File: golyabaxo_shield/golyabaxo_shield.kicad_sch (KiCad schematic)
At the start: 18 parts, among them J2 Conn_01x09, Q2 Q_NPN_BEC

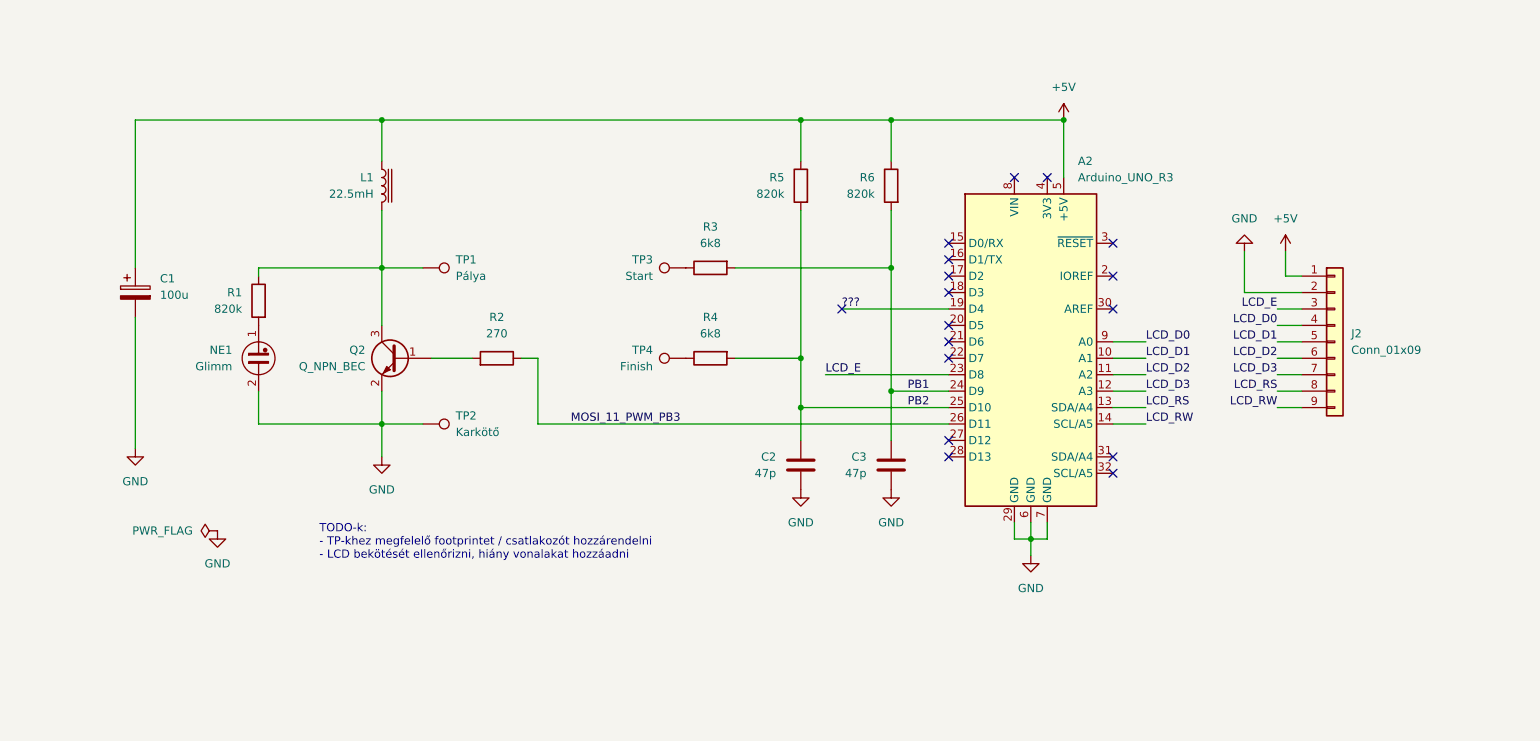
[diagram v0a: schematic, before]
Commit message: Add refurbished firmware for SEMduino-V2 - testing needed
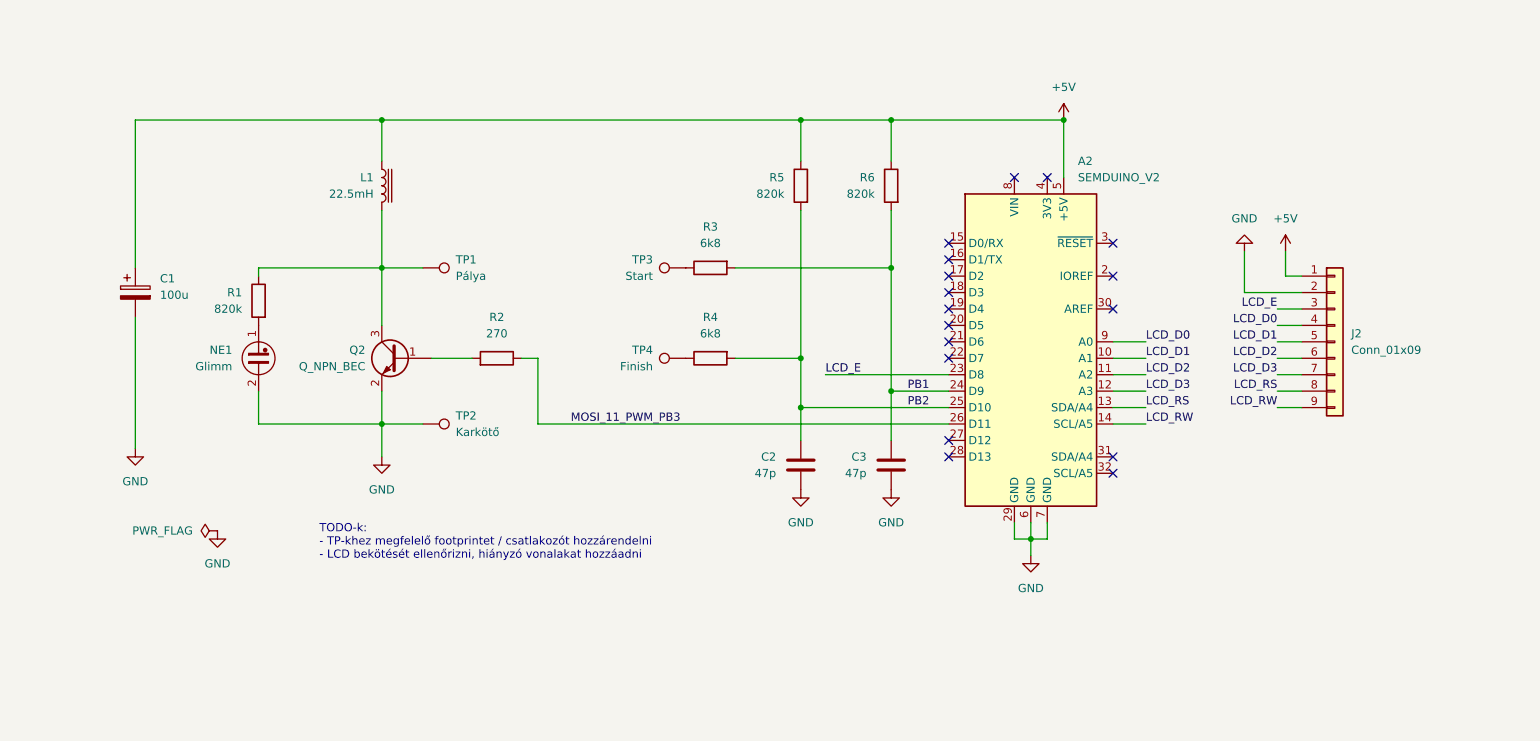
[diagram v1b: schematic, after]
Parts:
- A2: value Arduino_UNO_R3 -> SEMDUINO_V2
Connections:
- net ???: no longer names the net of A2.19 (D4)
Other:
- note added: "TODO-k: - TP-khez megfelelő footprintet / csatlakozót hozzárendelni - LCD bekötését ellenőrizni, hiányzó vonalakat hozzáadni"
- note removed: "TODO-k: - TP-khez megfelelő footprintet / csatlakozót hozzárendelni - LCD bekötését ellenőrizni, hiány vonalakat hozzáadni"
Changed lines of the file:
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@@
-	)
-	(no_connect
-		(at 163.83 92.71)
 	)
 	(no_connect
@@
 	)
 	(no_connect
+		(at 180.34 92.71)
+	)
+	(no_connect
 		(at 190.5 72.39)
 	)
@@
 	(wire
 		(pts
-			(xy 163.83 92.71) (xy 180.34 92.71)
-		)
-		(stroke
-			(width 0)
-			(type default)
-		)
-	)
-	(wire
-		(pts
 			(xy 231.14 92.71) (xy 234.95 92.71)
 		)
@@
 		)
 	)
-	(text "TODO-k:\n- TP-khez megfelelő footprintet / csatlakozót hozzárendelni\n- LCD bekötését ellenőrizni, hiány vonalakat hozzáadni"
+	(text "TODO-k:\n- TP-khez megfelelő footprintet / csatlakozót hozzárendelni\n- LCD bekötését ellenőrizni, hiányzó vonalakat hozzáadni"
 		(exclude_from_sim no)
 		(at 83.058 128.778 0)
@@
 	(label "PB2"
 		(at 173.99 107.95 0)
-		(fields_autoplaced yes)
-		(effects
-			(font
-				(size 1.27 1.27)
-			)
-			(justify left bottom)
-		)
-	)
-	(label "???"
-		(at 163.83 92.71 0)
 		(fields_autoplaced yes)
 		(effects
@@
 			)
 		)
-		(property "Value" "Arduino_UNO_R3"
+		(property "Value" "SEMDUINO_V2"
 			(at 200.3141 72.39 0)
 			(effects

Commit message: Build SEMduino shield
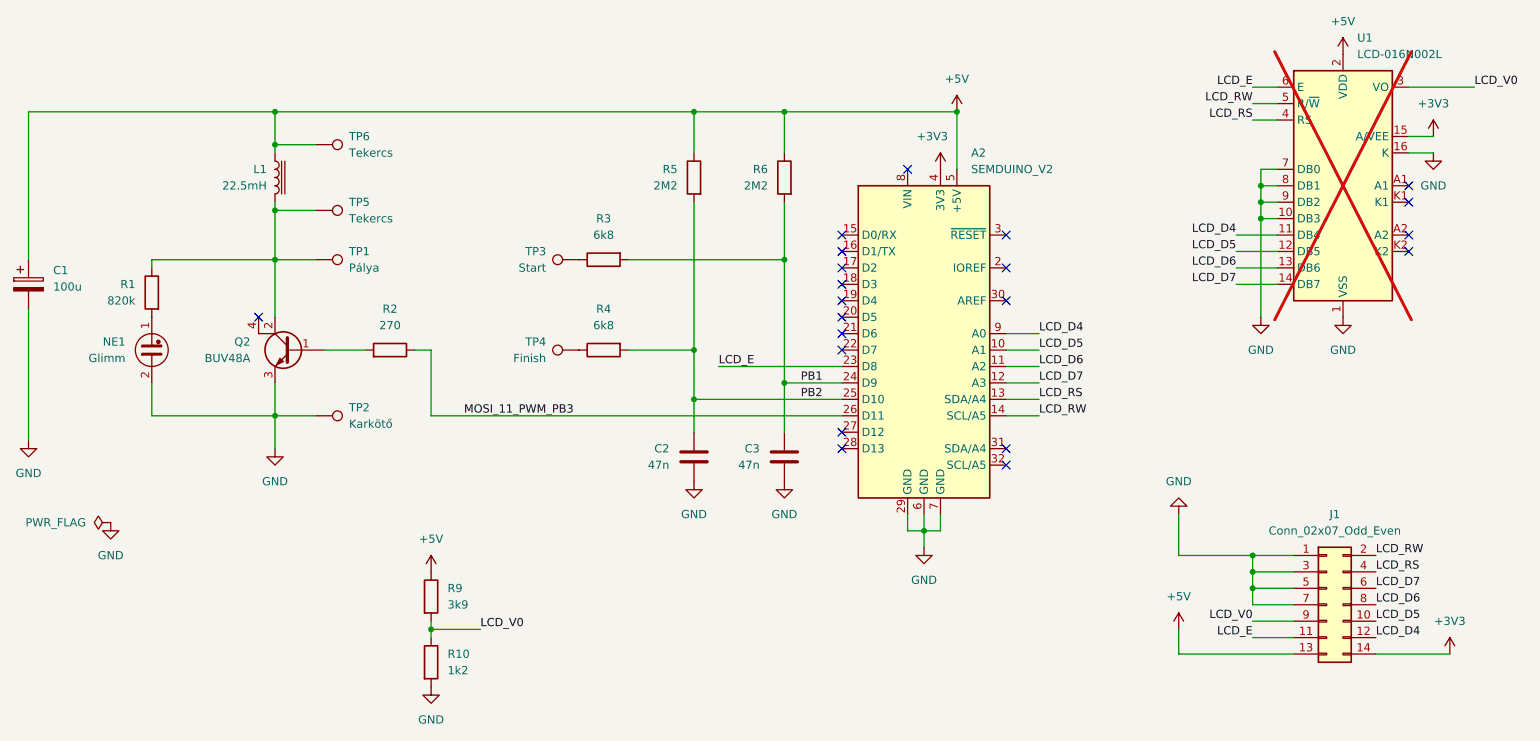
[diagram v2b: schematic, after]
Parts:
- removed J2: Conn_01x09, Connector_PinHeader_2.54mm:PinHeader_1x09_P2.54mm_Horizontal, symbol Connector_Generic:Conn_01x09
- removed Q2: Q_NPN_BEC, Package_TO_SOT_THT:TO-218-3_Horizontal_TabDown, symbol Device:Q_NPN_BEC
- added J1: Conn_02x07_Odd_Even, Connector_PinHeader_2.54mm:PinHeader_2x07_P2.54mm_Vertical_SMD, symbol Connector_Generic:Conn_02x07_Odd_Even
- added Q2: BUV48A, Package_TO_SOT_THT:TO-218-3_Horizontal_TabDown, symbol Device:Q_NPN_BCEC
- added R10: 1k2, Resistor_THT:R_Axial_DIN0207_L6.3mm_D2.5mm_P10.16mm_Horizontal, symbol Device:R
- added R9: 3k9, Resistor_THT:R_Axial_DIN0207_L6.3mm_D2.5mm_P10.16mm_Horizontal, symbol Device:R
- added TP5, TP6: Tekercs, TestPoint:TestPoint_Pad_D2.5mm, symbol Connector:TestPoint
- added U1: LCD-016N002L, Display:LCD-016N002L, symbol Display_Character:LCD-016N002L
- C2, C3: value 47p -> 47n; footprint Capacitor_THT:C_Disc_D4.3mm_W1.9mm_P5.00mm -> Capacitor_THT:C_Disc_D3.8mm_W2.6mm_P2.50mm
- L1: footprint Connector_PinHeader_2.54mm:PinHeader_1x02_P2.54mm_Horizontal -> (none)
- NE1: footprint LED_THT:LED_D5.0mm_Clear -> LED_THT:LED_D5.0mm_IRGrey
- R5, R6: value 820k -> 2M2
- TP1, TP2, TP3, TP4: footprint TestPoint:TestPoint_Loop_D2.50mm_Drill1.0mm -> TestPoint:TestPoint_Pad_D2.5mm
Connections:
- net +5V: now also J1.13 (Pin_13), R9.1, TP6.1, U1.2 (VDD)
- net GND: now also J1.1 (Pin_1), J1.3 (Pin_3), J1.5 (Pin_5), J1.7 (Pin_7), Q2.3 (E), R10.2, U1.1 (VSS), U1.10 (DB3), U1.16 (K), U1.7 (DB0), U1.8 (DB1), U1.9 (DB2)
- net LCD_E: now also J1.11 (Pin_11), U1.6 (E)
- net LCD_RS: now also J1.4 (Pin_4), U1.4 (RS)
- net LCD_RW: now also J1.2 (Pin_2), U1.5 (R/~{W})
- net at L1.1, R1.1, TP1.1: now also Q2.2 (C), TP5.1
- net at R2.2: now also Q2.1 (B)
- net +3V3: now reaches A2.4 (3V3)
- net +3V3: now also J1.14 (Pin_14), U1.15 (A/VEE)
- net LCD_D0 renamed LCD_D4
- net LCD_D4: now also J1.12 (Pin_12), U1.11 (DB4)
- net LCD_D1 renamed LCD_D5
- net LCD_D5: now also J1.10 (Pin_10), U1.12 (DB5)
- net LCD_D2 renamed LCD_D6
- net LCD_D6: now also J1.8 (Pin_8), U1.13 (DB6)
- net LCD_D3 renamed LCD_D7
- net LCD_D7: now also J1.6 (Pin_6), U1.14 (DB7)
- new net LCD_V0: J1.9 (Pin_9), R10.1, R9.2, U1.3 (VO)
- no-connect marks 17 -> 21
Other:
- note removed: "TODO-k: - TP-khez megfelelő footprintet / csatlakozót hozzárendelni - LCD bekötését ellenőrizni, hiányzó vonalakat hozzáadni"
- moved on the sheet: A2, C1, C2, C3, L1, NE1, R1, R2, R3, R4, R5, R6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
